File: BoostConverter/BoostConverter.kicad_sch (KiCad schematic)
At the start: 10 parts, among them U1 LT1370CR_TRPBF

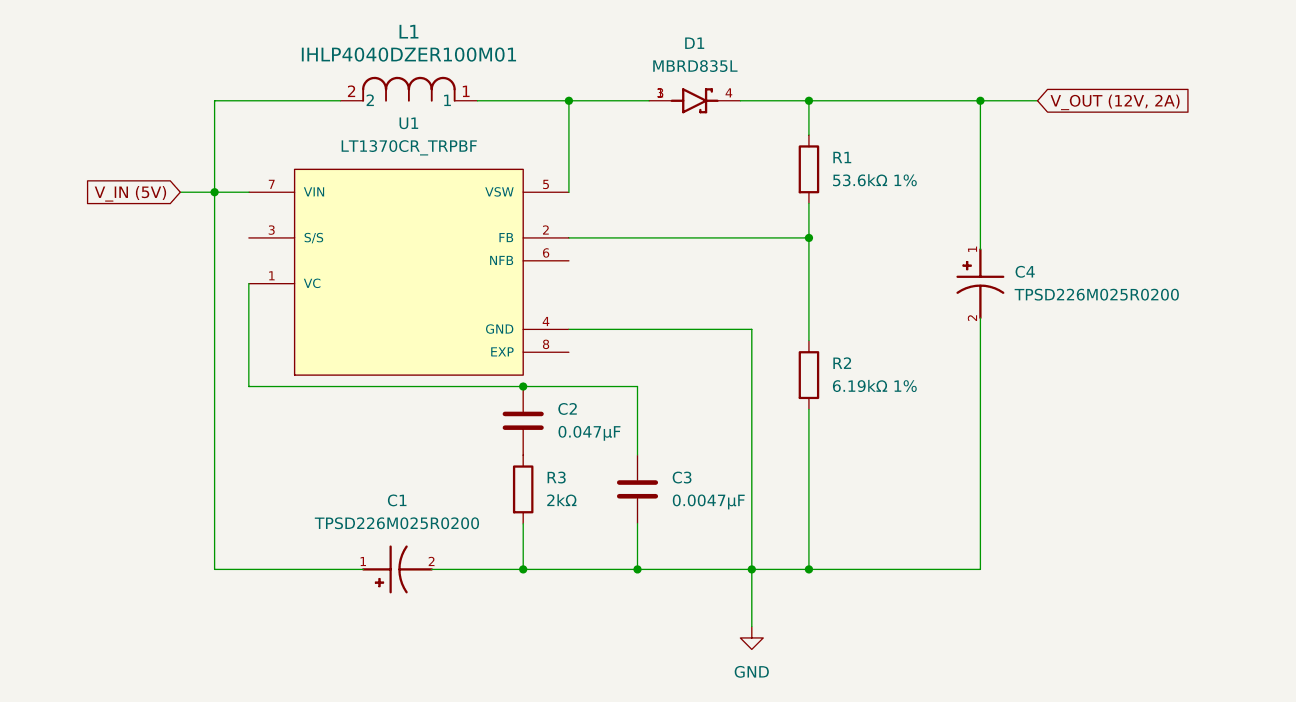
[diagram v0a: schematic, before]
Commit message: Re-did layout for Boost Converter
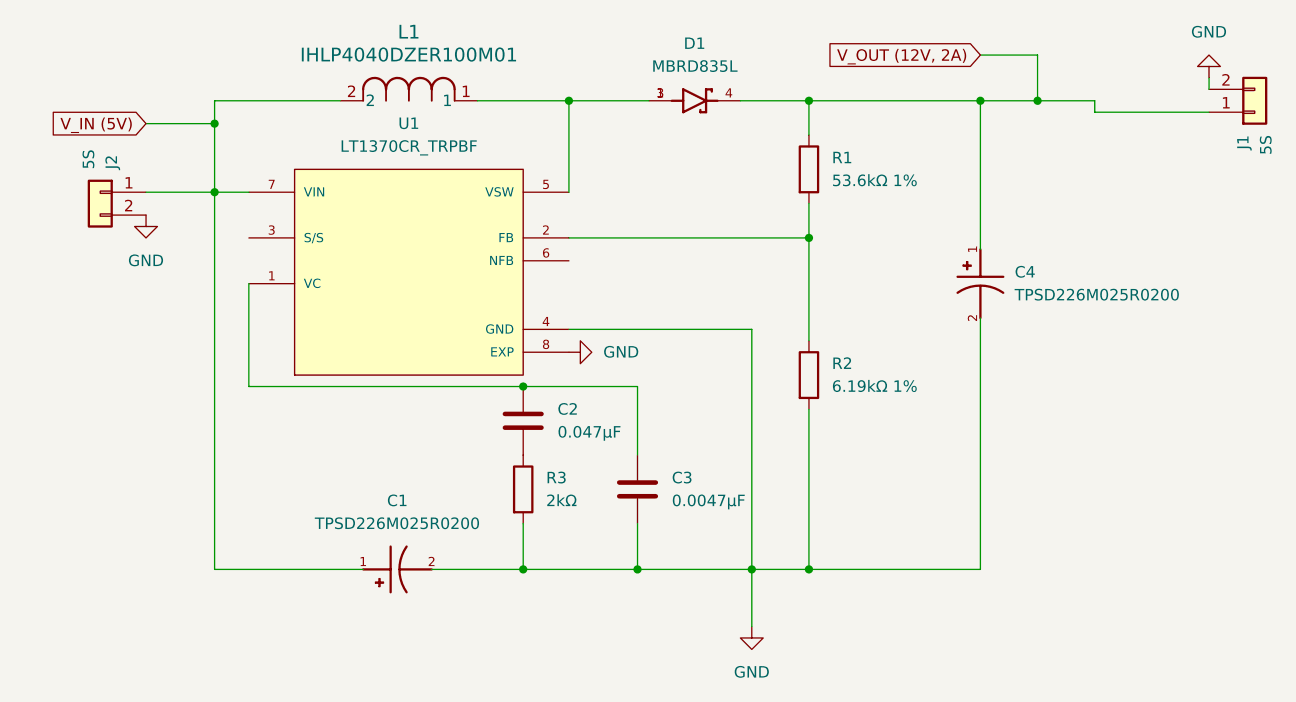
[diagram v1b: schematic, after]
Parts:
- added J1, J2: 5S, TerminalBlock_MetzConnect:TerminalBlock_MetzConnect_Type086_RT03403HBLC_1x03_P3.81mm_Horizontal, symbol Connector_Generic:Conn_01x02
- D1: footprint Package_TO_SOT_SMD:TO-252-3_TabPin2 -> Package_TO_SOT_SMD:TO-252-3_TabPin4
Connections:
- net GND: now also U1.8 (EXP), J1.2 (Pin_2), J2.2 (Pin_2)
- net V_IN (5V): now also J2.1 (Pin_1)
- net V_OUT (12V, 2A): now also J1.1 (Pin_1)
